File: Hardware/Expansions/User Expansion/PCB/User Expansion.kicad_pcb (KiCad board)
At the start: 2 copper layers, 100 x 70 mm, 867 parts, among them J101 10018784-10201TLF, U101 M24C02-FMN

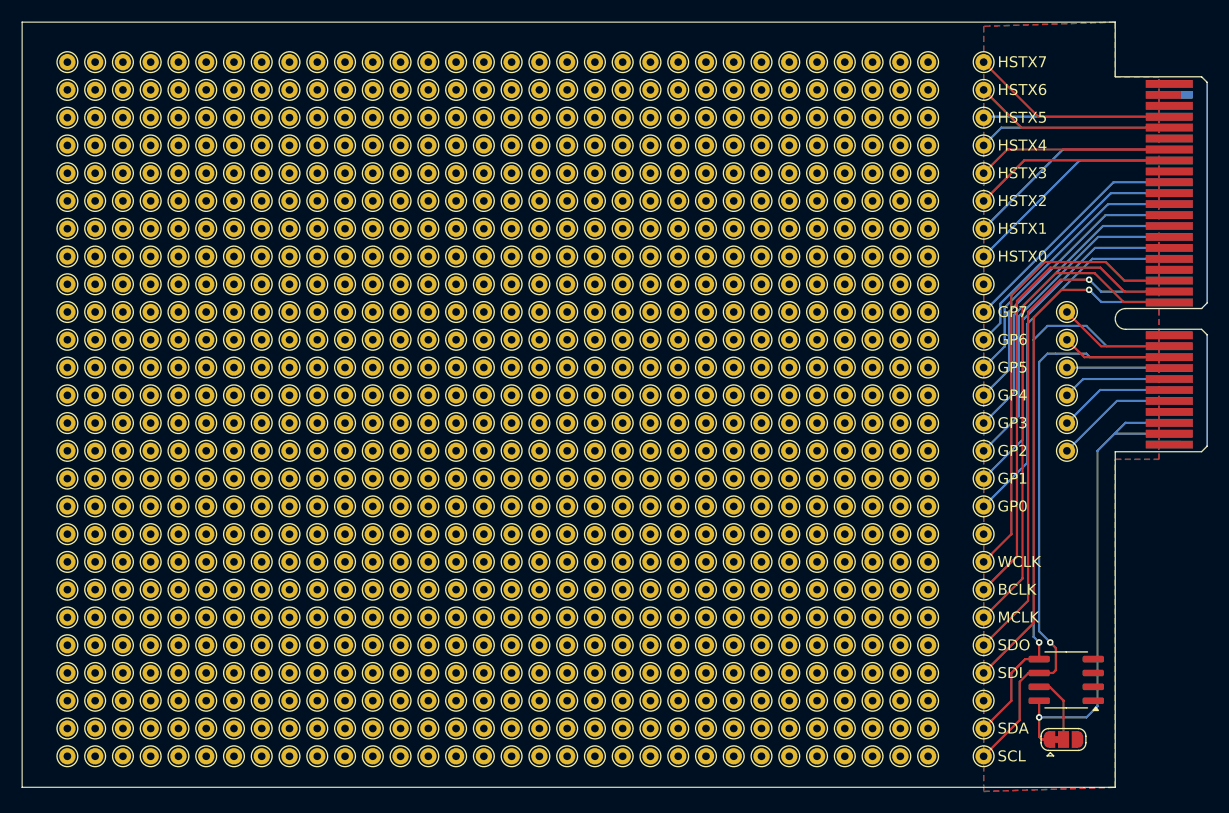
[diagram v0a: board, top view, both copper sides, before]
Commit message: Continues work on User Expansion design, adds CI for exports, ERC and DRC
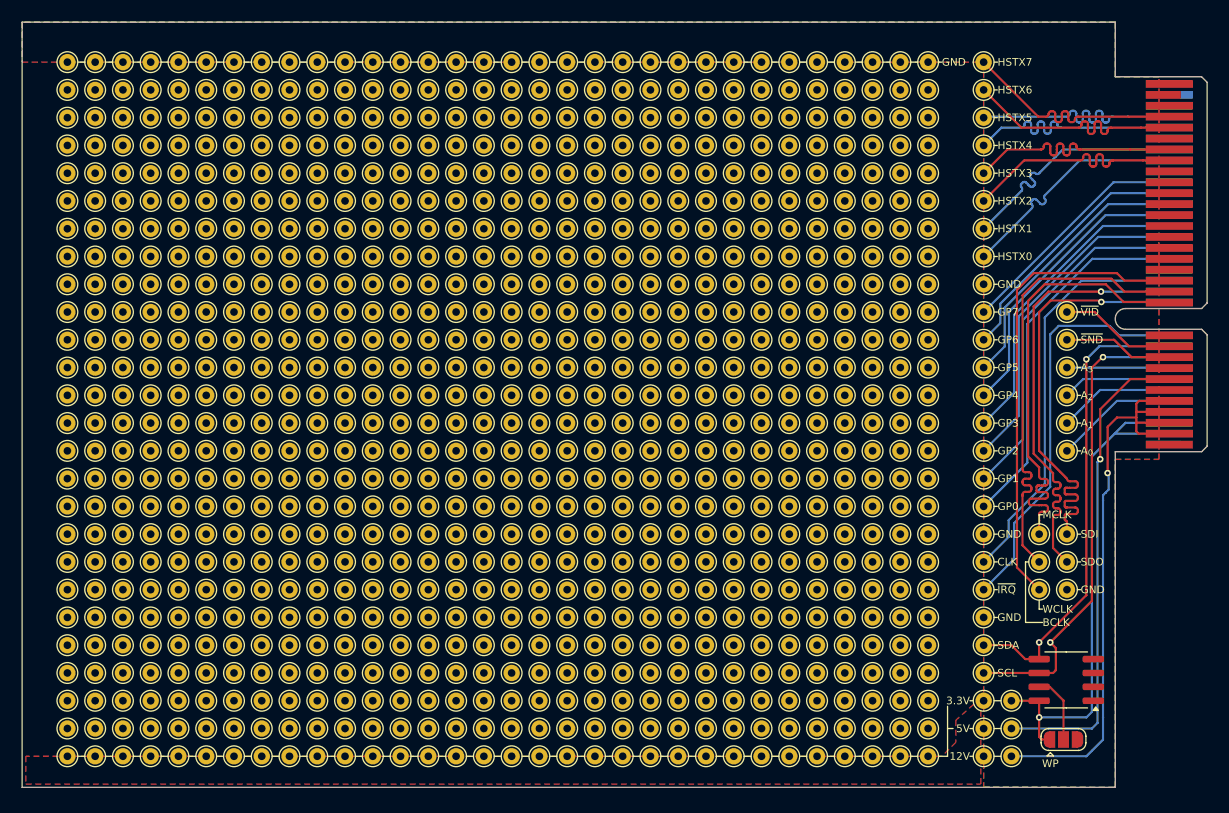
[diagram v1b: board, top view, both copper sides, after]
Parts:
- removed TP1433, TP1434, TP1435, TP1436, TP1437, TP1438, TP1439, TP1440, TP1441, TP1442, TP1443, TP1444, TP1445, TP1446, TP1447, TP1448, TP1449, TP1450, TP1451, TP1452, TP1453, TP1454, TP1455, TP1456, TP1457, TP1458, TP1459, TP1460, TP1461, TP1462, TP1463, TP1464: -, TestPoint:TestPoint_THTPad_D1.5mm_Drill0.7mm
- added TP1301: -, TestPoint:TestPoint_THTPad_D1.5mm_Drill0.7mm, F.Cu at (172.7, 73.7)
- added TP1302: -, TestPoint:TestPoint_THTPad_D1.5mm_Drill0.7mm, F.Cu at (160.0, 73.7)
- added TP1303: -, TestPoint:TestPoint_THTPad_D1.5mm_Drill0.7mm, F.Cu at (147.3, 73.7)
- added TP1304: -, TestPoint:TestPoint_THTPad_D1.5mm_Drill0.7mm, F.Cu at (134.6, 73.7)
- added TP1305: -, TestPoint:TestPoint_THTPad_D1.5mm_Drill0.7mm, F.Cu at (124.5, 73.7)
- added TP1306: -, TestPoint:TestPoint_THTPad_D1.5mm_Drill0.7mm, F.Cu at (114.3, 73.7)
- added TP1307: -, TestPoint:TestPoint_THTPad_D1.5mm_Drill0.7mm, F.Cu at (104.1, 73.7)
- added TP1308: -, TestPoint:TestPoint_THTPad_D1.5mm_Drill0.7mm, F.Cu at (175.3, 73.7)
- added TP1309: -, TestPoint:TestPoint_THTPad_D1.5mm_Drill0.7mm, F.Cu at (162.6, 73.7)
- added TP1310: -, TestPoint:TestPoint_THTPad_D1.5mm_Drill0.7mm, F.Cu at (149.9, 73.7)
- added TP1311: -, TestPoint:TestPoint_THTPad_D1.5mm_Drill0.7mm, F.Cu at (137.2, 73.7)
- added TP1312: -, TestPoint:TestPoint_THTPad_D1.5mm_Drill0.7mm, F.Cu at (127.0, 73.7)
- added TP1313: -, TestPoint:TestPoint_THTPad_D1.5mm_Drill0.7mm, F.Cu at (116.8, 73.7)
- added TP1314: -, TestPoint:TestPoint_THTPad_D1.5mm_Drill0.7mm, F.Cu at (106.7, 73.7)
- added TP1315: -, TestPoint:TestPoint_THTPad_D1.5mm_Drill0.7mm, F.Cu at (177.8, 73.7)
- added TP1316: -, TestPoint:TestPoint_THTPad_D1.5mm_Drill0.7mm, F.Cu at (165.1, 73.7)
- added TP1317: -, TestPoint:TestPoint_THTPad_D1.5mm_Drill0.7mm, F.Cu at (152.4, 73.7)
- added TP1318: -, TestPoint:TestPoint_THTPad_D1.5mm_Drill0.7mm, F.Cu at (139.7, 73.7)
- added TP1319: -, TestPoint:TestPoint_THTPad_D1.5mm_Drill0.7mm, F.Cu at (129.5, 73.7)
- added TP1320: -, TestPoint:TestPoint_THTPad_D1.5mm_Drill0.7mm, F.Cu at (119.4, 73.7)
- added TP1321: -, TestPoint:TestPoint_THTPad_D1.5mm_Drill0.7mm, F.Cu at (109.2, 73.7)
- added TP1322: -, TestPoint:TestPoint_THTPad_D1.5mm_Drill0.7mm, F.Cu at (180.3, 73.7)
- added TP1323: -, TestPoint:TestPoint_THTPad_D1.5mm_Drill0.7mm, F.Cu at (167.6, 73.7)
- added TP1324: -, TestPoint:TestPoint_THTPad_D1.5mm_Drill0.7mm, F.Cu at (154.9, 73.7)
- added TP1325: -, TestPoint:TestPoint_THTPad_D1.5mm_Drill0.7mm, F.Cu at (142.2, 73.7)
- added TP1326: -, TestPoint:TestPoint_THTPad_D1.5mm_Drill0.7mm, F.Cu at (132.1, 73.7)
- added TP1327: -, TestPoint:TestPoint_THTPad_D1.5mm_Drill0.7mm, F.Cu at (121.9, 73.7)
- added TP1328: -, TestPoint:TestPoint_THTPad_D1.5mm_Drill0.7mm, F.Cu at (111.8, 73.7)
- added TP1329: -, TestPoint:TestPoint_THTPad_D1.5mm_Drill0.7mm, F.Cu at (182.9, 73.7)
- added TP133: GP7, TestPoint:TestPoint_THTPad_D1.5mm_Drill0.7mm, F.Cu at (195.6, 121.9)
- added TP1330: -, TestPoint:TestPoint_THTPad_D1.5mm_Drill0.7mm, F.Cu at (170.2, 73.7)
- added TP1331: -, TestPoint:TestPoint_THTPad_D1.5mm_Drill0.7mm, F.Cu at (157.5, 73.7)
- added TP1332: -, TestPoint:TestPoint_THTPad_D1.5mm_Drill0.7mm, F.Cu at (144.8, 73.7)
- added TP134: GP7, TestPoint:TestPoint_THTPad_D1.5mm_Drill0.7mm, F.Cu at (188.0, 116.8)
- added TP135: GP7, TestPoint:TestPoint_THTPad_D1.5mm_Drill0.7mm, F.Cu at (188.0, 132.1)
- added TP136: GP7, TestPoint:TestPoint_THTPad_D1.5mm_Drill0.7mm, F.Cu at (188.0, 124.5)
- added TP137: GP7, TestPoint:TestPoint_THTPad_D1.5mm_Drill0.7mm, F.Cu at (188.0, 134.6)
- added TP138: GP7, TestPoint:TestPoint_THTPad_D1.5mm_Drill0.7mm, F.Cu at (188.0, 137.2)
- added TP139: GP7, TestPoint:TestPoint_THTPad_D1.5mm_Drill0.7mm, F.Cu at (190.5, 134.6)
- added TP140: GP7, TestPoint:TestPoint_THTPad_D1.5mm_Drill0.7mm, F.Cu at (190.5, 137.2)
- added TP141: GP7, TestPoint:TestPoint_THTPad_D1.5mm_Drill0.7mm, F.Cu at (190.5, 132.1)
- JP101: footprint Jumper:SolderJumper-3_P1.3mm_Bridged12_RoundedPad1.0x1.5mm -> Jumper:SolderJumper-3_P1.3mm_Open_RoundedPad1.0x1.5mm
- moved TP1415 66.1 mm to (109.2, 137.2)
- moved TP1421 63.6 mm to (180.3, 137.2)
- moved TP1003 61.0 mm to (147.3, 134.6)
- moved TP1005 61.0 mm to (154.9, 134.6)
- moved TP1009 61.0 mm to (144.8, 134.6)
- moved TP1021 61.0 mm to (157.5, 134.6)
- moved TP1033 61.0 mm to (149.9, 134.6)
- moved TP1037 61.0 mm to (160.0, 134.6)
- moved TP1049 61.0 mm to (152.4, 134.6)
- moved TP1053 61.0 mm to (162.6, 134.6)
- moved TP203 61.0 mm to (106.7, 134.6)
- moved TP205 61.0 mm to (114.3, 134.6)
- moved TP209 61.0 mm to (104.1, 134.6)
- moved TP221 61.0 mm to (116.8, 134.6)
- moved TP233 61.0 mm to (109.2, 134.6)
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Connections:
- TP101 pad 1: unconnected-(TP101-Pad1) -> GND
- TP1401 pad 1: unconnected-(TP1401-Pad1) -> /Connected Row1/COM
- TP1402 pad 1: unconnected-(TP1402-Pad1) -> /Connected Row1/COM
- TP1403 pad 1: unconnected-(TP1403-Pad1) -> /Connected Row1/COM
- TP1404 pad 1: unconnected-(TP1404-Pad1) -> /Connected Row1/COM
- TP1405 pad 1: unconnected-(TP1405-Pad1) -> /Connected Row1/COM
- TP1406 pad 1: unconnected-(TP1406-Pad1) -> /Connected Row1/COM
- TP1407 pad 1: unconnected-(TP1407-Pad1) -> /Connected Row1/COM
- TP1408 pad 1: unconnected-(TP1408-Pad1) -> /Connected Row1/COM
- TP1409 pad 1: unconnected-(TP1409-Pad1) -> /Connected Row1/COM
- TP1410 pad 1: unconnected-(TP1410-Pad1) -> /Connected Row1/COM
- TP1411 pad 1: unconnected-(TP1411-Pad1) -> /Connected Row1/COM
- TP1412 pad 1: unconnected-(TP1412-Pad1) -> /Connected Row1/COM
- TP1413 pad 1: unconnected-(TP1413-Pad1) -> /Connected Row1/COM
- TP1414 pad 1: unconnected-(TP1414-Pad1) -> /Connected Row1/COM
- TP1415 pad 1: unconnected-(TP1415-Pad1) -> /Connected Row1/COM
- TP1416 pad 1: unconnected-(TP1416-Pad1) -> /Connected Row1/COM
- TP1417 pad 1: unconnected-(TP1417-Pad1) -> /Connected Row1/COM
- TP1418 pad 1: unconnected-(TP1418-Pad1) -> /Connected Row1/COM
- TP1419 pad 1: unconnected-(TP1419-Pad1) -> /Connected Row1/COM
- TP1420 pad 1: unconnected-(TP1420-Pad1) -> /Connected Row1/COM
- TP1421 pad 1: unconnected-(TP1421-Pad1) -> /Connected Row1/COM
- TP1422 pad 1: unconnected-(TP1422-Pad1) -> /Connected Row1/COM
- TP1423 pad 1: unconnected-(TP1423-Pad1) -> /Connected Row1/COM
- TP1424 pad 1: unconnected-(TP1424-Pad1) -> /Connected Row1/COM
- TP1425 pad 1: unconnected-(TP1425-Pad1) -> /Connected Row1/COM
- TP1426 pad 1: unconnected-(TP1426-Pad1) -> /Connected Row1/COM
- TP1427 pad 1: unconnected-(TP1427-Pad1) -> /Connected Row1/COM
- TP1428 pad 1: unconnected-(TP1428-Pad1) -> /Connected Row1/COM
- TP1429 pad 1: unconnected-(TP1429-Pad1) -> /Connected Row1/COM
- TP1430 pad 1: unconnected-(TP1430-Pad1) -> /Connected Row1/COM
- TP1431 pad 1: unconnected-(TP1431-Pad1) -> /Connected Row1/COM
- TP1432 pad 1: unconnected-(TP1432-Pad1) -> /Connected Row1/COM
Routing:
- net +12V: track 0.00 -> 55.7 mm, vias 0 -> 1
- net +5V: track 0.00 -> 44.4 mm, vias 0 -> 1
- net Net-(J101-CLK_{16MHz}): track 0.00 -> 37.5 mm
- net Net-(J101-~{IRQ}): track 0.00 -> 37.5 mm
- net /SCL: track 53.1 -> 43.7 mm, vias 1 -> 2
- net /SDA: track 52.3 -> 42.9 mm, vias 1 -> 2
- net Net-(J101-I²S_{SDIN}): track 48.3 -> 39.9 mm
- net Net-(J101-I²S_{SDOUT}): track 46.8 -> 40.3 mm
- net Net-(J101-HSTX_{5}): track 17.0 -> 21.9 mm
- net Net-(J101-HSTX_{4}): track 17.7 -> 21.9 mm
- net Net-(J101-HSTX_{3}): track 17.9 -> 21.9 mm
- net Net-(J101-I²S_{MCLK}): track 45.7 -> 41.9 mm
- net Net-(J101-HSTX_{6}): track 18.4 -> 21.9 mm
- net Net-(J101-HSTX_{2}): track 18.5 -> 21.9 mm
- net Net-(J101-HSTX_{7}): track 19.1 -> 21.9 mm
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- added copper zone on F.Cu, net /Connected Row1/COM
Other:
- board text added: "12V"
- board text added: "3.3V"
- board text added: "5V"
- board text added: "A_{0}"
- board text added: "A_{1}"
- board text added: "A_{2}"
- board text added: "A_{3}"
- board text added: "CLK"
- board text added: "GND"
- board text added: "WP"
- board text added: "~{IRQ}"
- board text added: "~{SND}"
- board text added: "~{VID}"
